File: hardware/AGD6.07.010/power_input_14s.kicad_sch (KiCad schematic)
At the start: 31 parts, among them J101 PDB_14S XT30, Q101 100V N-MOSFET >=40A D2PAK (на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, U101 LM5069MM-1, U102 INA228AIDGSR

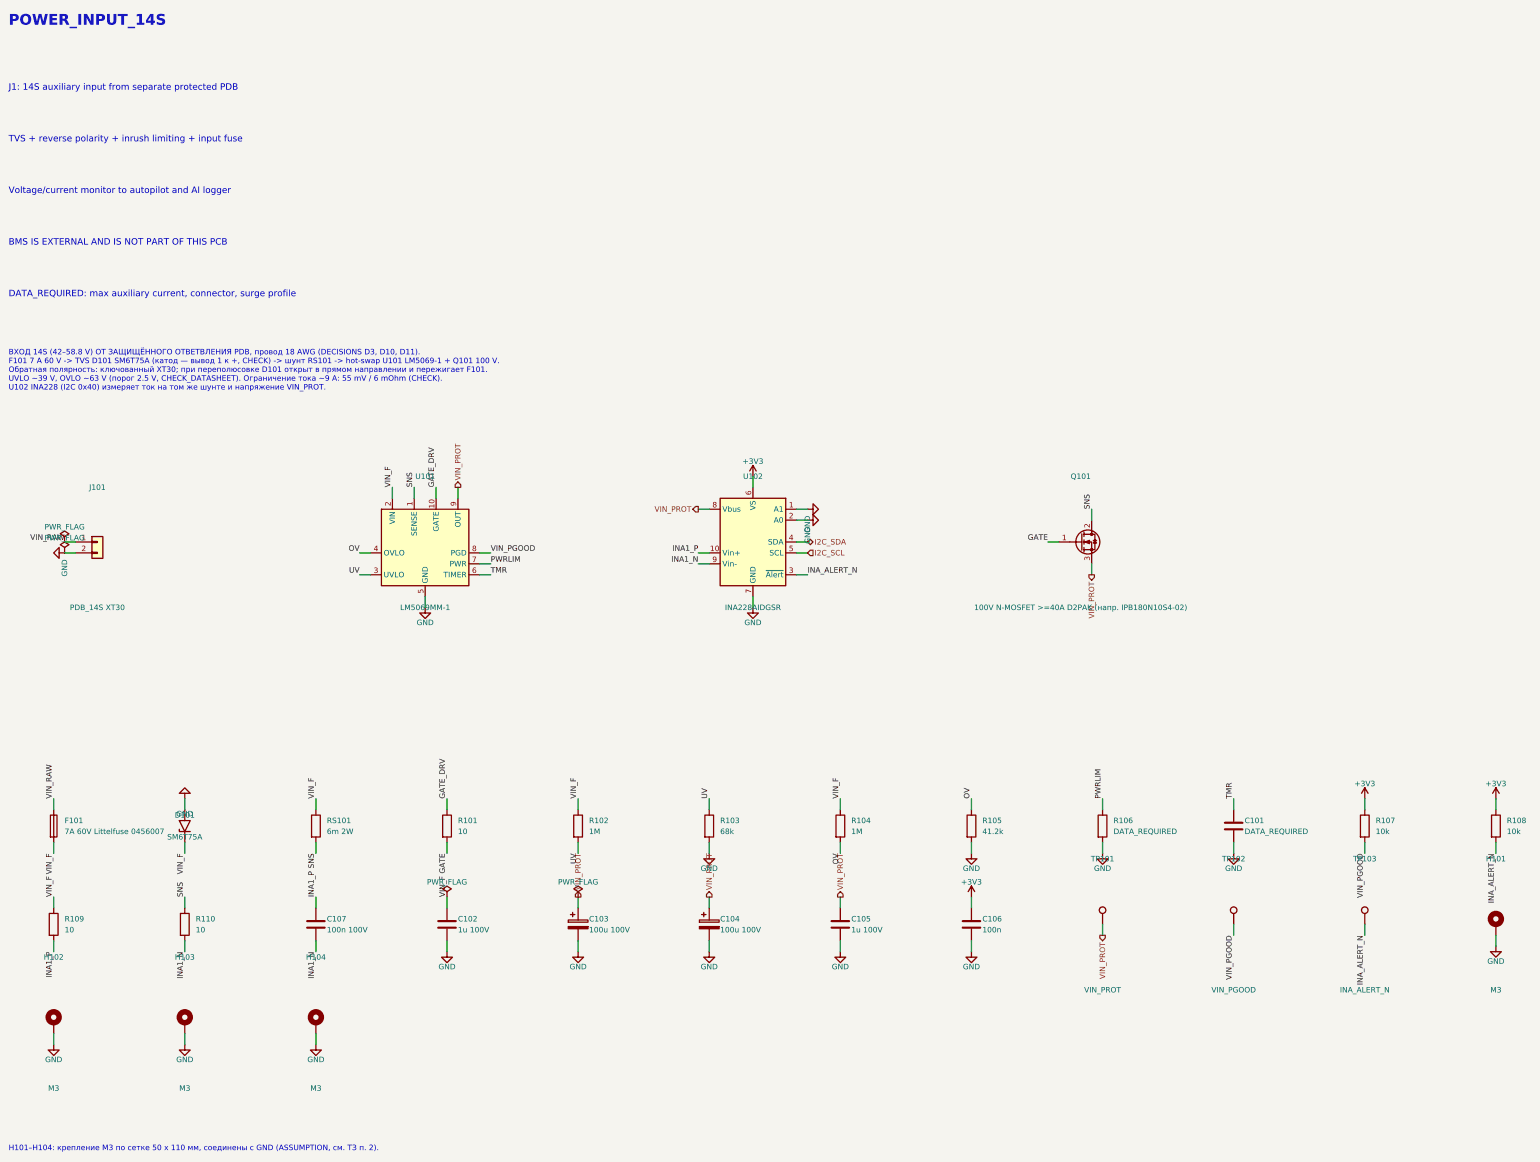
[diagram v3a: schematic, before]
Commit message: AGD6.07.010 rev 0.4 (WIP): 3x TRACO THL40 DC/DC, split 12 V bus, SwitchBlox Ethernet, fixed LM5069 UVLO/OVLO, computed hot-swap values, PX4 firmware notes; board re-placed, routing in progress
Co-Authored-By: Claude Opus 5.5 <noreply@anthropic.com>
Claude-Session: https://claude.ai/code/session_01Qk7uTKdi6YbndB9fGuguYV
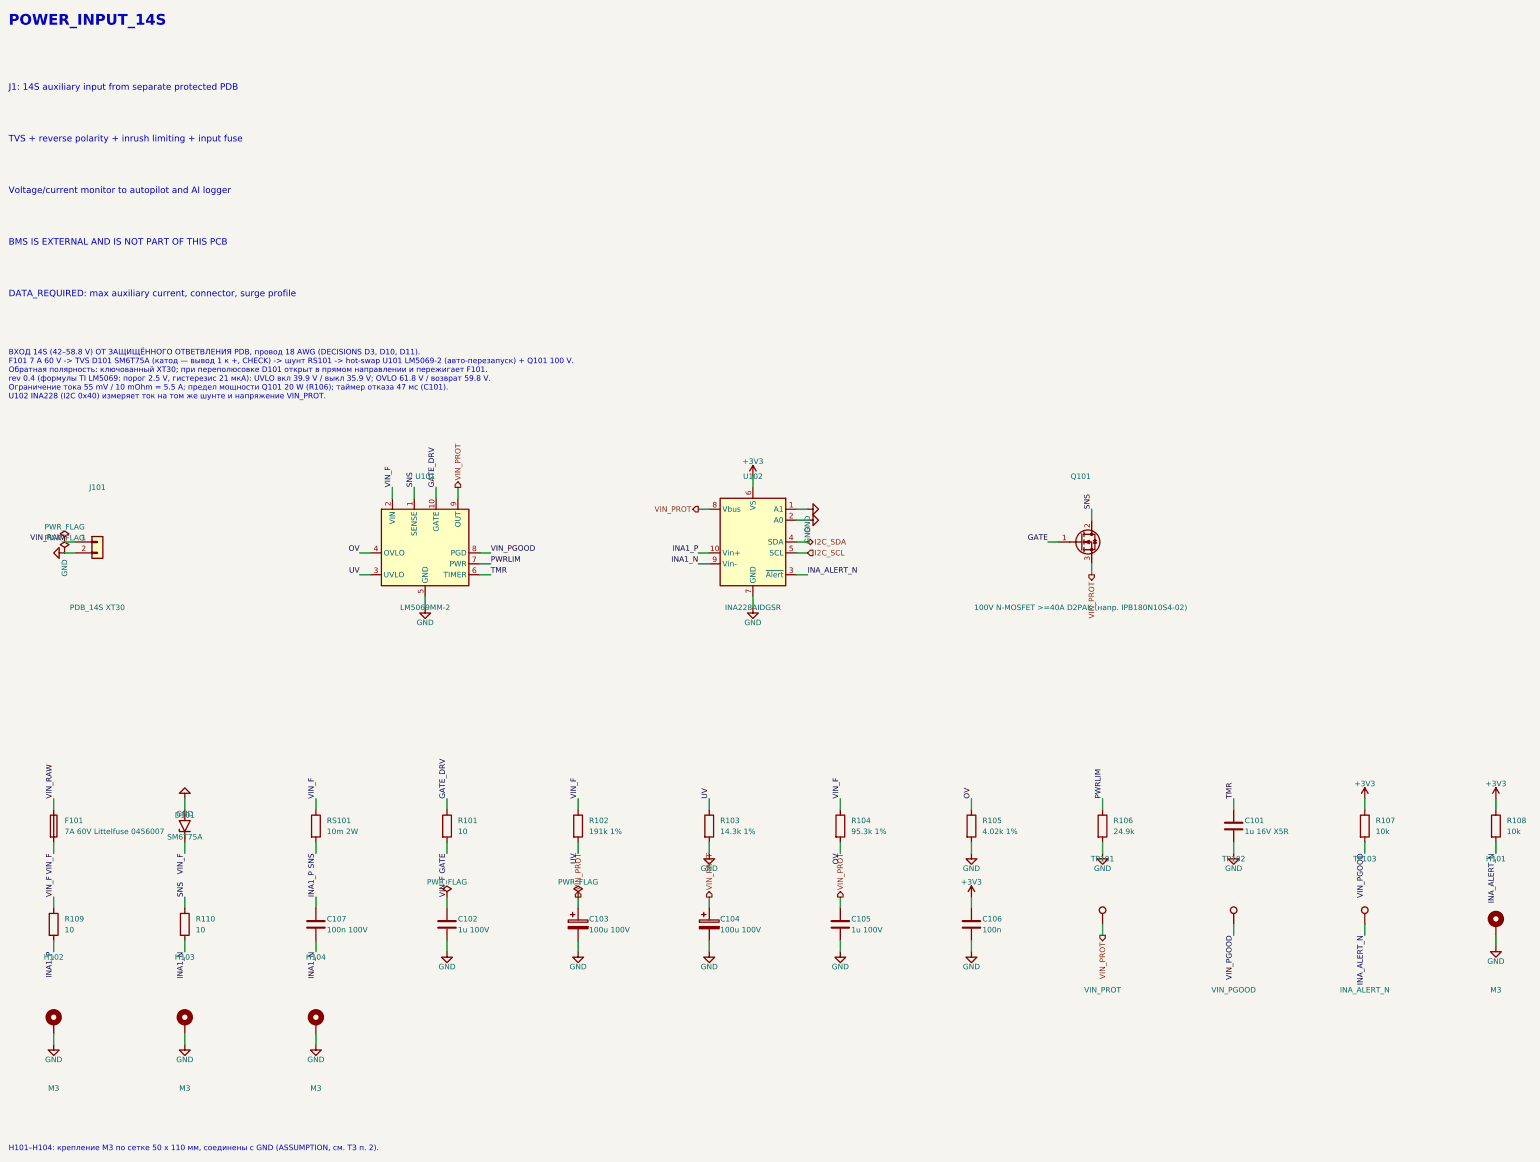
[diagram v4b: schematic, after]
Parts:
- removed U101: LM5069MM-1, Package_SO:MSOP-10_3x3mm_P0.5mm, symbol Power_Management:LM5069MM-1
- added U101: LM5069MM-2, Package_SO:MSOP-10_3x3mm_P0.5mm, symbol Power_Management:LM5069MM-2
- C101: value DATA_REQUIRED -> 1u 16V X5R; Note CHECK_DATASHEET -> РАСЧЁТ: calculations.md; Purpose таймер отказа -> t_fault = C x 4 V / 85 uA = 47 ms
- R102: value 1M -> 191k 1%; Note CHECK_DATASHEET -> РАСЧЁТ: calculations.md; Purpose (none) -> UVLO: R1 = (39.9-35.9 V)/21 uA
- R103: value 68k -> 14.3k 1%; Note CHECK_DATASHEET -> РАСЧЁТ: calculations.md; Purpose (none) -> UVLO: R2 = 2.5 V x R1 / (35.9 - 2.5 V)
- R104: value 1M -> 95.3k 1%; Note CHECK_DATASHEET -> РАСЧЁТ: calculations.md; Purpose (none) -> OVLO: R3 = (61.8-59.8 V)/21 uA
- R105: value 41.2k -> 4.02k 1%; Note CHECK_DATASHEET -> РАСЧЁТ: calculations.md; Purpose (none) -> OVLO: R4 = 2.5 V x R3 / (61.8 - 2.5 V)
- R106: value DATA_REQUIRED -> 24.9k; Note CHECK_DATASHEET -> РАСЧЁТ: calculations.md; Purpose предел мощности FET -> P_LIM Q101 = 20 W: R = 1.25e5 x 0.010 x 20
- RS101: value 6m 2W -> 10m 2W; Note CHECK_DATASHEET -> РАСЧЁТ: calculations.md
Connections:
- net GATE_DRV: now also U101.10 (GATE)
- net GND: now also U101.5 (GND)
- net OV: now also U101.4 (OVLO)
- net PWRLIM: now also U101.7 (PWR)
- net SNS: now also U101.1 (SENSE)
- net TMR: now also U101.6 (TIMER)
- net UV: now also U101.3 (UVLO)
- net VIN_F: now also U101.2 (VIN)
- net VIN_PGOOD: now also U101.8 (PGD)
- net VIN_PROT: now also U101.9 (OUT)
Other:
- note added: "ВХОД 14S (42–58.8 V) ОТ ЗАЩИЩЁННОГО ОТВЕТВЛЕНИЯ PDB, провод 18 AWG (DECISIONS D3, D10, D11). F101 7 A 60 V -> TVS D101 SM6T75A (катод — вывод 1 к +, CHECK) -> шунт RS101 -> hot-swap U101 LM5069-2 (авто-перезапуск) + Q101 100 V. Обратная полярность: ключованный XT30; при переполюсовке D101 открыт в прямом направлении и пережигает F101. rev 0.4 (формулы TI LM5069: порог 2.5 V, гистерезис 21 мкА): U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"
- note removed: "ВХОД 14S (42–58.8 V) ОТ ЗАЩИЩЁННОГО ОТВЕТВЛЕНИЯ PDB, провод 18 AWG (DECISIONS D3, D10, D11). F101 7 A 60 V -> TVS D101 SM6T75A (катод — вывод 1 к +, CHECK) -> шунт RS101 -> hot-swap U101 LM5069-1 + Q101 100 V. Обратная полярность: ключованный XT30; при переполюсовке D101 открыт в прямом направлении и пережигает F101. UVLO ~39 V, OVLO ~63 V (порог 2.5 V, CHECK_DATASHEET). Ограничение тока ~9 A: 55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"
